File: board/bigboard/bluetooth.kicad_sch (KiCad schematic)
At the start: 2 parts, among them J4 Conn_01x03_Male, U3 D52MxxM8

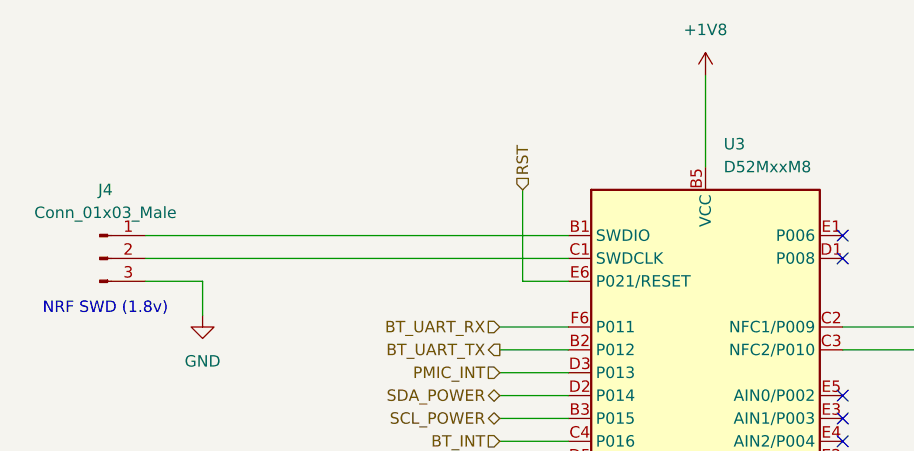
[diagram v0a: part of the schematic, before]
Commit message: Manufactured version of bigboard
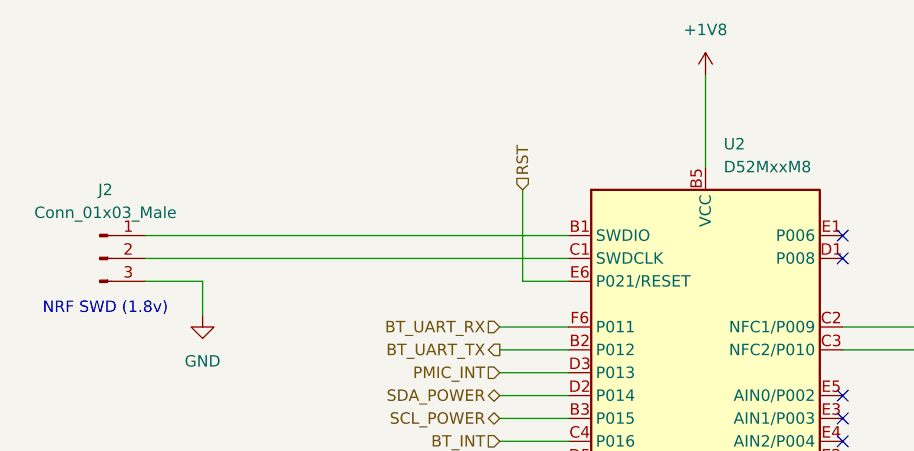
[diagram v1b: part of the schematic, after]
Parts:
- renumbered J4 to J2, U3 to U2
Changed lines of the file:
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@@
   (symbol (lib_id "power:GND") (at 144.78 143.51 0) (unit 1)
     (in_bom yes) (on_board yes) (fields_autoplaced)
-    (property "Reference" "#PWR017" (id 0) (at 144.78 149.86 0)
+    (property "Reference" "#PWR013" (id 0) (at 144.78 149.86 0)
       (effects (font (size 1.27 1.27)) hide)
     )
@@
   (symbol (lib_id "power:+1V8") (at 144.78 63.5 0) (unit 1)
     (in_bom yes) (on_board yes) (fields_autoplaced)
-    (property "Reference" "#PWR016" (id 0) (at 144.78 67.31 0)
+    (property "Reference" "#PWR012" (id 0) (at 144.78 67.31 0)
       (effects (font (size 1.27 1.27)) hide)
     )
@@
   (symbol (lib_id "RF_Module:D52MxxM8") (at 144.78 99.06 0) (unit 1)
     (in_bom yes) (on_board yes) (fields_autoplaced)
-    (property "Reference" "U3" (id 0) (at 146.7994 71.12 0)
+    (property "Reference" "U2" (id 0) (at 146.7994 71.12 0)
       (effects (font (size 1.27 1.27)) (justify left))
     )
@@
   (symbol (lib_id "power:GND") (at 88.9 90.17 0) (unit 1)
     (in_bom yes) (on_board yes) (fields_autoplaced)
-    (property "Reference" "#PWR015" (id 0) (at 88.9 96.52 0)
+    (property "Reference" "#PWR011" (id 0) (at 88.9 96.52 0)
       (effects (font (size 1.27 1.27)) hide)
     )
@@
   (symbol (lib_id "Connector:Conn_01x03_Male") (at 77.47 83.82 0) (unit 1)
     (in_bom yes) (on_board yes) (fields_autoplaced)
-    (property "Reference" "J4" (id 0) (at 78.105 76.2 0))
+    (property "Reference" "J2" (id 0) (at 78.105 76.2 0))
     (property "Value" "Conn_01x03_Male" (id 1) (at 78.105 78.74 0))
     (property "Footprint" "Connector_PinHeader_2.54mm:PinHeader_1x03_P2.54mm_Vertical" (id 2) (at 77.47 83.82 0)

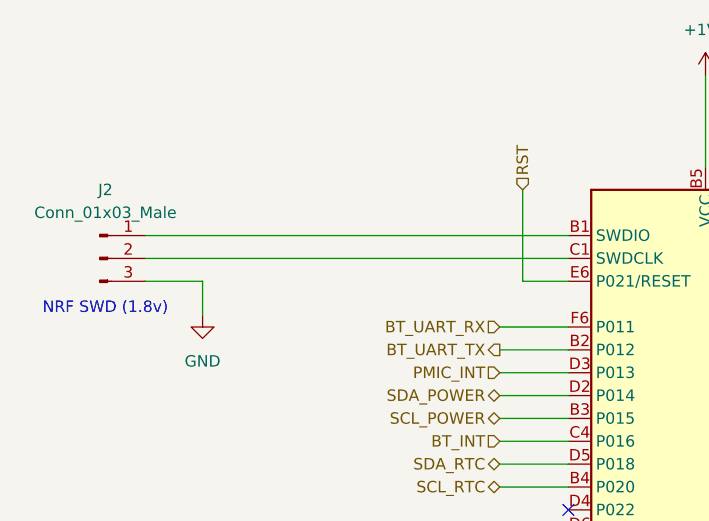
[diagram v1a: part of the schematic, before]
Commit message: Update board to kicad 7
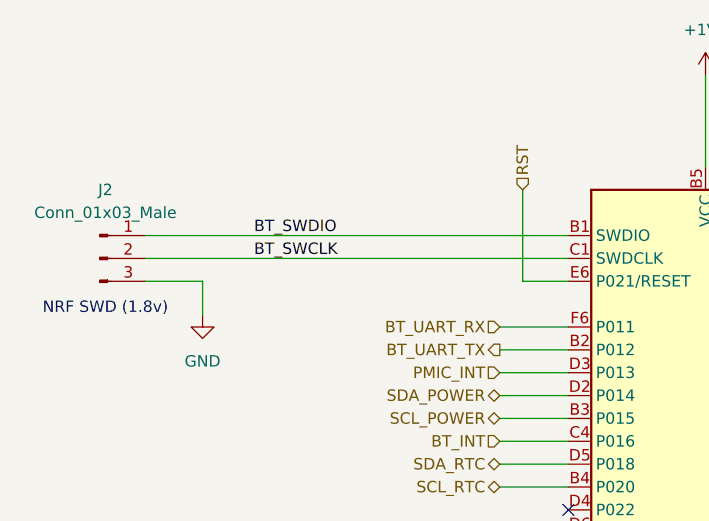
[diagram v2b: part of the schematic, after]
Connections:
- net BT_SWDIO: now reaches J2.1 (Pin_1), U2.B1 (SWDIO)
- net BT_SWCLK: now reaches J2.2 (Pin_2), U2.C1 (SWDCLK)
